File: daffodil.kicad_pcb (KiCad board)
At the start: 2 copper layers, 70.7 x 53.3 mm, 8 parts, among them J1 NEIGHBOR1, J2 NEIGHBOR2, J7 BONUS_ROW, P1 GREATFET-PROTO-AREA

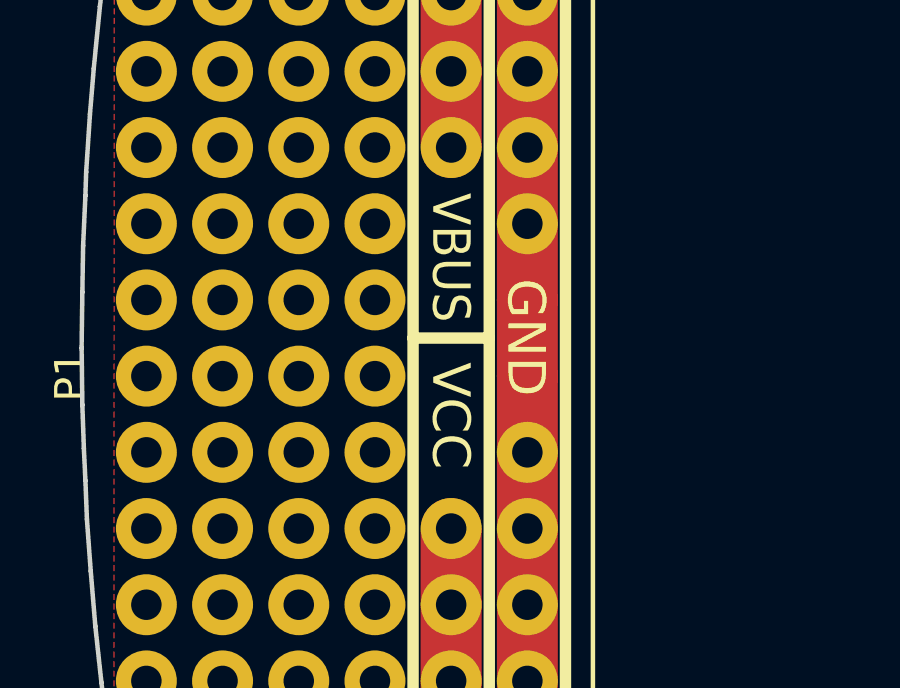
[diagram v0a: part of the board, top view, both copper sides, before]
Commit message: Resolved issue #1
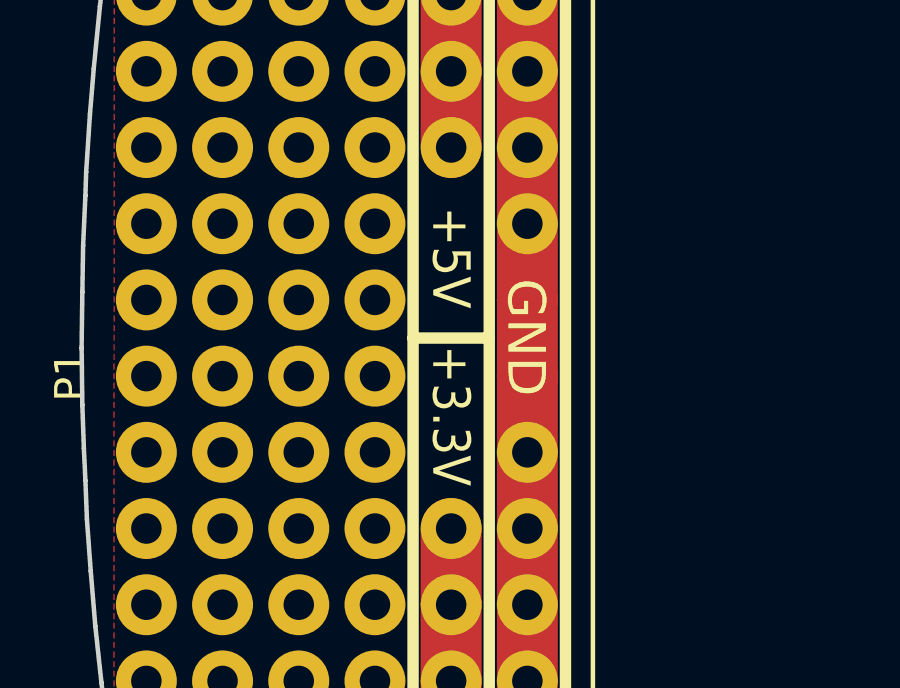
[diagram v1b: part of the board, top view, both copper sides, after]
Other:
- board text added: "+3.3V"
- board text added: "+5V"
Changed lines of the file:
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@@
-(kicad_pcb (version 20171130) (host pcbnew 5.1.2-f72e74a~84~ubuntu18.04.1)
+(kicad_pcb (version 20171130) (host pcbnew 5.1.4-e60b266~84~ubuntu18.04.1)
   (general
     (thickness 1.6)
@@
     (effects (font (size 0.635 0.508) (thickness 0.1016)))
   )
-  (gr_text VCC (at 121.9 97.84 270) (layer F.SilkS)
-    (effects (font (size 1.25 1.25) (thickness 0.225)))
-  )
-  (gr_text VBUS (at 121.9 92.57 270) (layer F.SilkS)
+  (gr_text +3.3V (at 121.9 97.84 270) (layer F.SilkS)
+    (effects (font (size 1.25 1.1) (thickness 0.21)))
+  )
+  (gr_text +5V (at 121.9 92.57 270) (layer F.SilkS)
     (effects (font (size 1.25 1.15) (thickness 0.225)))
   )

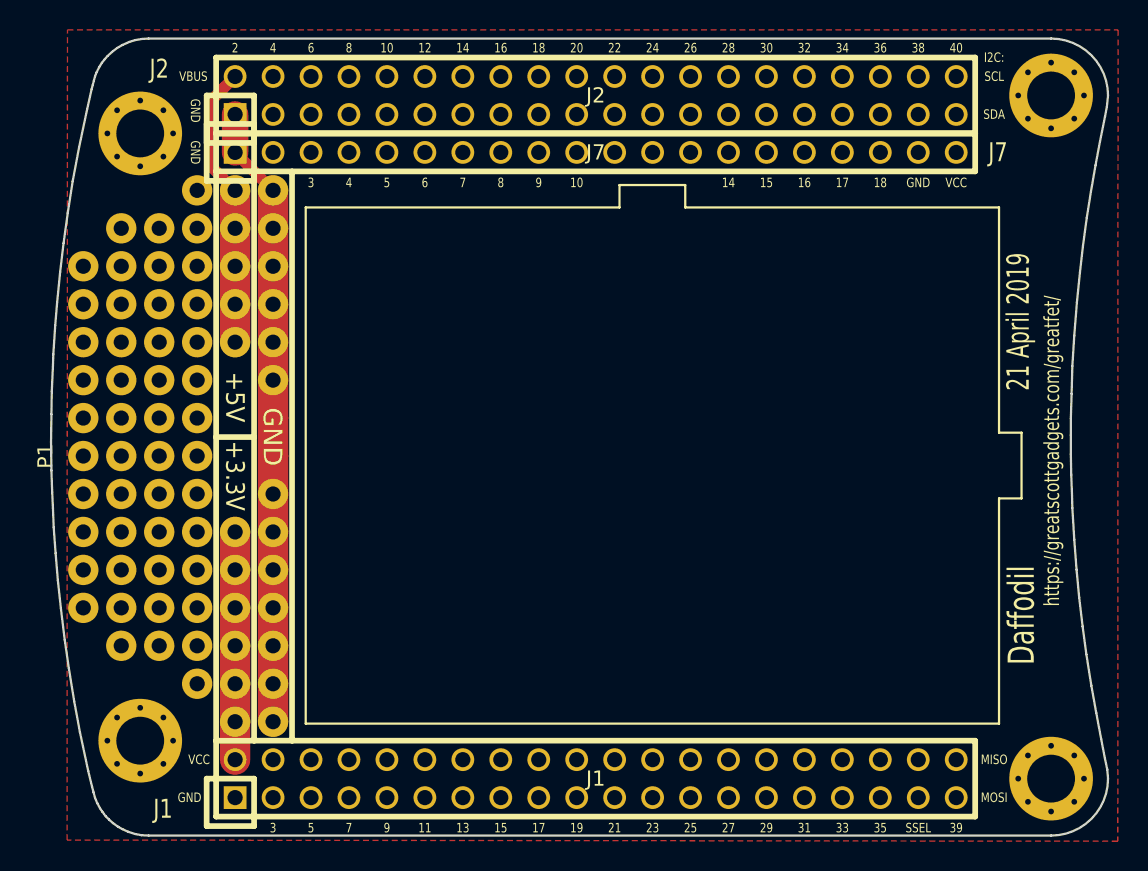
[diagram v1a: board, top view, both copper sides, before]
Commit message: Corrected 5V/3.3V markings on silkscreen
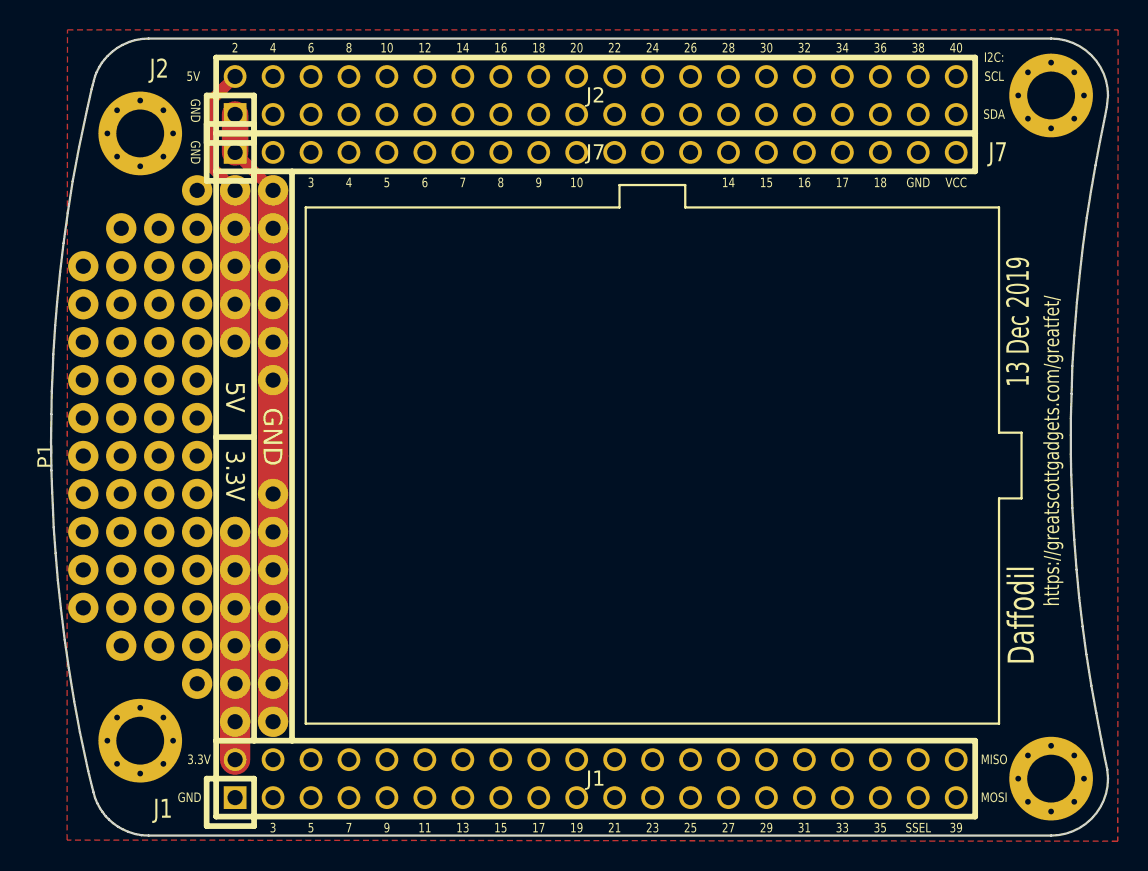
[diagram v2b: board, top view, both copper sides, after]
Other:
- board text added: "13 Dec 2019"
- board text added: "3.3V"
- board text added: "5V"
- board text removed: "+3.3V"
- board text removed: "+5V"
- board text removed: "21 April 2019"
- board text removed: "VBUS"
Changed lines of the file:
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@@
-(kicad_pcb (version 20171130) (host pcbnew 5.1.4-e60b266~84~ubuntu18.04.1)
+(kicad_pcb (version 20171130) (host pcbnew 5.1.5-52549c5~84~ubuntu18.04.1)
   (general
     (thickness 1.6)
@@
     (effects (font (size 0.635 0.508) (thickness 0.1016)))
   )
-  (gr_text +3.3V (at 121.9 97.84 270) (layer F.SilkS)
+  (gr_text 3.3V (at 121.9 97.84 270) (layer F.SilkS)
     (effects (font (size 1.25 1.1) (thickness 0.21)))
   )
-  (gr_text +5V (at 121.9 92.57 270) (layer F.SilkS)
+  (gr_text 5V (at 121.9 92.57 270) (layer F.SilkS)
     (effects (font (size 1.25 1.15) (thickness 0.225)))
   )
@@
   (gr_line (start 177.9016 92.3544) (end 177.8508 94.0054) (angle 90) (layer Edge.Cuts) (width 0.15))
   (gr_line (start 177.9524 90.5002) (end 177.9016 92.3544) (angle 90) (layer Edge.Cuts) (width 0.15))
-  (gr_text "21 April 2019" (at 174.34 87.53 90) (layer F.SilkS)
+  (gr_text "13 Dec 2019" (at 174.34 87.53 90) (layer F.SilkS)
     (effects (font (size 1.5 1) (thickness 0.2)))
   )
@@
     (effects (font (size 0.635 0.508) (thickness 0.1016)))
   )
-  (gr_text VBUS (at 119.126 71.12) (layer F.SilkS)
-    (effects (font (size 0.635 0.508) (thickness 0.1016)))
-  )
-  (gr_text VCC (at 119.507 116.84) (layer F.SilkS)
-    (effects (font (size 0.635 0.508) (thickness 0.1016)))
-  )
+  (gr_text 5V (at 119.126 71.12) (layer F.SilkS)
+    (effects (font (size 0.635 0.508) (thickness 0.1016)))
+  )
+  (gr_text 3.3V (at 119.507 116.84) (layer F.SilkS)
+    (effects (font (size 0.635 0.508) (thickness 0.1016)))
+  )

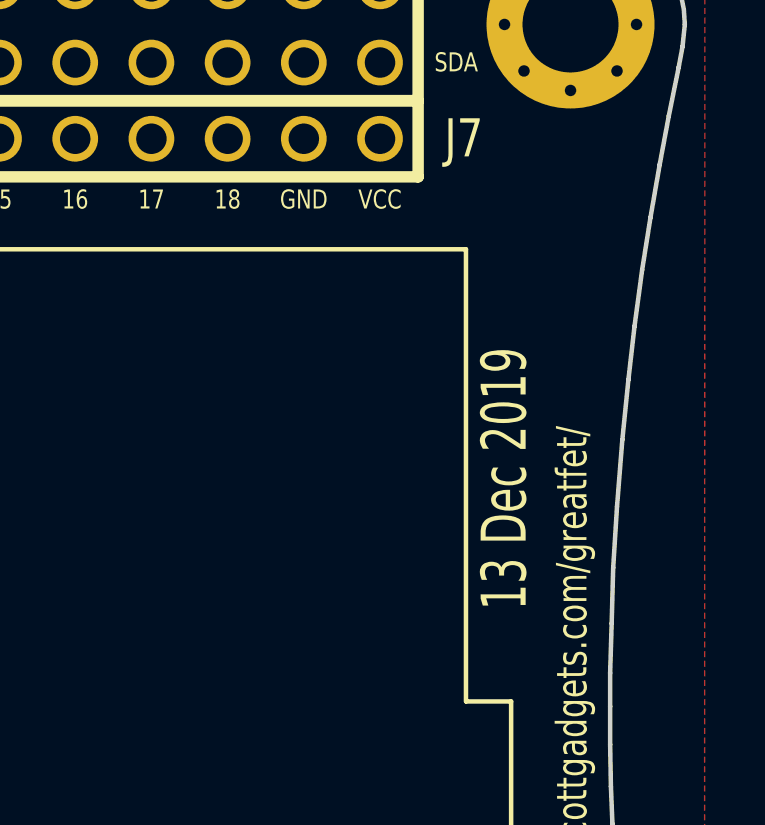
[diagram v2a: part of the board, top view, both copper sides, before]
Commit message: update net names in layout to match schematic fix one last VCC on silkscreen to match 3.3V used elsewhere
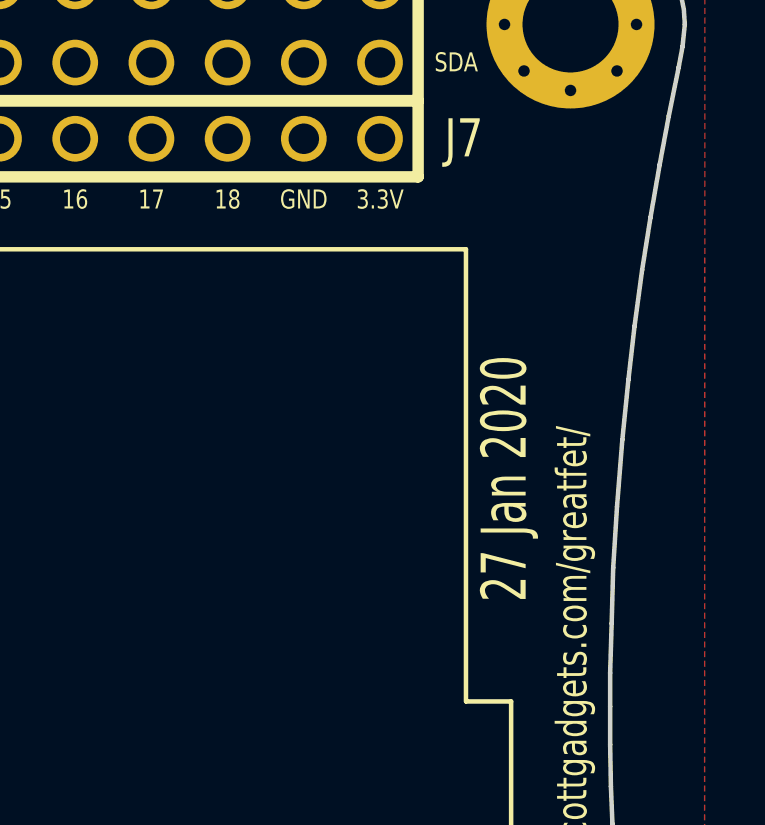
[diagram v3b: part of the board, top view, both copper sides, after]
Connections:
- net /VBUS renamed +5V
- net VCC renamed +3V3
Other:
- board text added: "27 Jan 2020"
- board text removed: "13 Dec 2019"
- board text removed: "VCC"
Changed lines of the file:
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@@
   (net 0 "")
   (net 1 GND)
-  (net 2 VCC)
-  (net 3 /VBUS)
+  (net 2 +3V3)
+  (net 3 +5V)
   (net 4 /P4_9)
   (net 5 /P0_0)
@@
     (add_net /RTC_ALARM)
     (add_net /VBAT)
-    (add_net /VBUS)
+    (add_net +5V)
     (add_net /WAKEUP0)
     (add_net GND)
@@
     (add_net "Net-(P1-Pad71)")
     (add_net "Net-(P1-Pad72)")
-    (add_net VCC)
+    (add_net +3V3)
   )
   (module gsg-modules:HEADER-1x20 (layer F.Cu)
@@
       (net 1 GND))
     (pad 20 thru_hole circle (at 24.13 0) (size 1.524 1.524) (drill 1.016) (layers *.Cu *.Mask F.SilkS)
-      (net 2 VCC))
+      (net 2 +3V3))
   )
   (module gsg-modules:HEADER-2x20 (layer F.Cu)
@@
       (net 1 GND) (die_length 0.08382))
     (pad 2 thru_hole circle (at -24.13 -1.27) (size 1.524 1.524) (drill 1.016) (layers *.Cu *.Mask F.SilkS)
-      (net 2 VCC) (die_length -1518.485687))
+      (net 2 +3V3) (die_length -1518.485687))
     (pad 3 thru_hole circle (at -21.59 1.27) (size 1.524 1.524) (drill 1.016) (layers *.Cu *.Mask F.SilkS)
       (net 4 /P4_9) (die_length 0.06096))
@@
       (net 1 GND) (die_length 0.08382))
     (pad 2 thru_hole circle (at -24.13 -1.27) (size 1.524 1.524) (drill 1.016) (layers *.Cu *.Mask F.SilkS)
-      (net 3 /VBUS) (die_length -1518.485687))
+      (net 3 +5V) (die_length -1518.485687))
     (pad 3 thru_hole circle (at -21.59 1.27) (size 1.524 1.524) (drill 1.016) (layers *.Cu *.Mask F.SilkS)
       (net 42 /P4_8) (die_length 0.06096))
@@
       (net 1 GND))
     (pad 14 thru_hole circle (at -2.54 -17.78) (size 2.032 2.032) (drill 1.016) (layers *.Cu *.Mask F.SilkS)
-      (net 3 /VBUS))
+      (net 3 +5V))
     (pad 15 thru_hole circle (at -2.54 -15.24) (size 2.032 2.032) (drill 1.016) (layers *.Cu *.Mask F.SilkS)
-      (net 3 /VBUS))
+      (net 3 +5V))
     (pad 16 thru_hole circle (at -2.54 -12.7) (size 2.032 2.032) (drill 1.016) (layers *.Cu *.Mask F.SilkS)
-      (net 3 /VBUS))
+      (net 3 +5V))
     (pad 17 thru_hole circle (at -2.54 -10.16) (size 2.032 2.032) (drill 1.016) (layers *.Cu *.Mask F.SilkS)
-      (net 3 /VBUS))
+      (net 3 +5V))
     (pad 18 thru_hole circle (at -2.54 -7.62) (size 2.032 2.032) (drill 1.016) (layers *.Cu *.Mask F.SilkS)
-      (net 3 /VBUS))
+      (net 3 +5V))
     (pad 19 thru_hole circle (at -2.54 5.08) (size 2.032 2.032) (drill 1.016) (layers *.Cu *.Mask F.SilkS)
-      (net 2 VCC))
+      (net 2 +3V3))
     (pad 20 thru_hole circle (at -2.54 7.62) (size 2.032 2.032) (drill 1.016) (layers *.Cu *.Mask F.SilkS)
-      (net 2 VCC))
+      (net 2 +3V3))
     (pad 21 thru_hole circle (at -2.54 10.16) (size 2.032 2.032) (drill 1.016) (layers *.Cu *.Mask F.SilkS)
-      (net 2 VCC))
+      (net 2 +3V3))
     (pad 22 thru_hole circle (at -2.54 12.7) (size 2.032 2.032) (drill 1.016) (layers *.Cu *.Mask F.SilkS)
-      (net 2 VCC))
+      (net 2 +3V3))
     (pad 23 thru_hole circle (at -2.54 15.24) (size 2.032 2.032) (drill 1.016) (layers *.Cu *.Mask F.SilkS)
-      (net 2 VCC))
+      (net 2 +3V3))
     (pad 24 thru_hole circle (at -2.54 17.78) (size 2.032 2.032) (drill 1.016) (layers *.Cu *.Mask F.SilkS)
-      (net 2 VCC))
+      (net 2 +3V3))
     (pad 25 thru_hole circle (at -5.08 -17.78) (size 2.032 2.032) (drill 1.016) (layers *.Cu *.Mask F.SilkS)
       (net 135 "Net-(P1-Pad25)"))
@@
     (effects (font (size 0.635 0.508) (thickness 0.1016)))
   )
-  (gr_text VCC (at 170.18 78.232) (layer F.SilkS)
+  (gr_text 3.3V (at 170.18 78.232) (layer F.SilkS)
     (effects (font (size 0.635 0.508) (thickness 0.1016)))
   )
@@
   (gr_line (start 177.9016 92.3544) (end 177.8508 94.0054) (angle 90) (layer Edge.Cuts) (width 0.15))
   (gr_line (start 177.9524 90.5002) (end 177.9016 92.3544) (angle 90) (layer Edge.Cuts) (width 0.15))
-  (gr_text "13 Dec 2019" (at 174.34 87.53 90) (layer F.SilkS)
+  (gr_text "27 Jan 2020" (at 174.34 87.53 90) (layer F.SilkS)
     (effects (font (size 1.5 1) (thickness 0.2)))
   )
@@
   (segment (start 121.92 81.28) (end 121.92 83.82) (width 2.032) (layer F.Cu) (net 3))
   (segment (start 121.92 78.74) (end 121.92 81.28) (width 2.032) (layer F.Cu) (net 3))
-  (zone (net 2) (net_name VCC) (layer In2.Cu) (hatch edge 0.508)
+  (zone (net 2) (net_name +3V3) (layer In2.Cu) (hatch edge 0.508)
     (connect_pads (clearance 0.254))
     (min_thickness 0.254)
